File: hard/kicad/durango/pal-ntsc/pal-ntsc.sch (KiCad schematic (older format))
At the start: 34 parts, among them J101 SCART, J103 ~CSYNC, J4 S-Video, J5 COMPOSITE, Q1 BC548, Q2 BC548, Q3 BC548, U1 AD724, Y1 3.58 MHz (PAL=4.43)

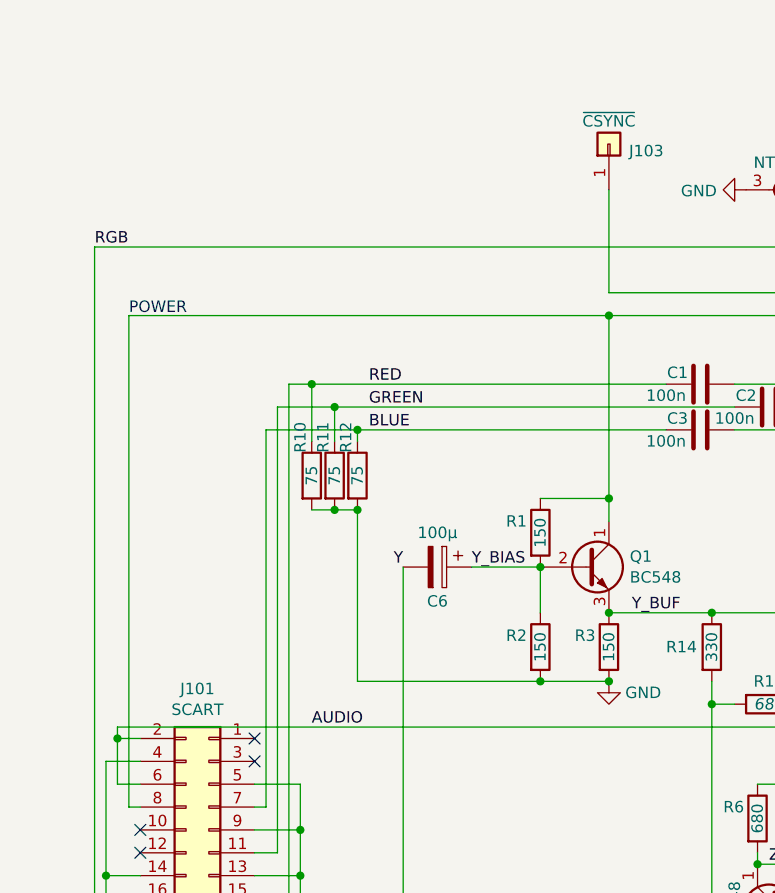
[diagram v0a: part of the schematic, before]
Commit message: preliminary PAL/NTSC encoder layout
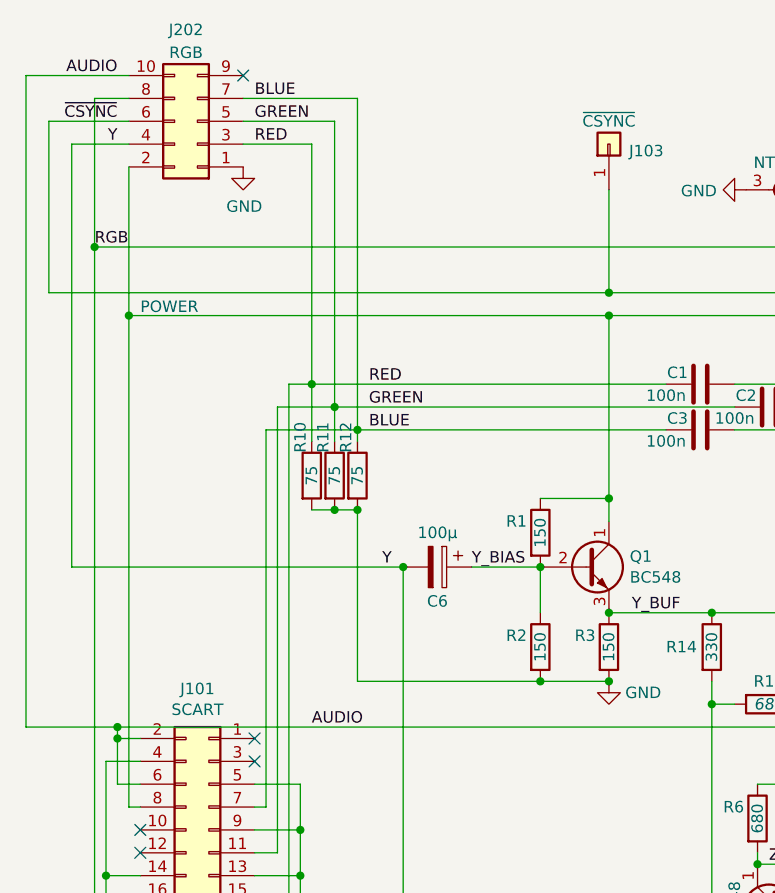
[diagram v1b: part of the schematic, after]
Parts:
- added J202: RGB, Connector_PinHeader_2.54mm:PinHeader_2x05_P2.54mm_Horizontal, symbol Connector_Generic:Conn_02x05_Odd_Even
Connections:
- net +5V: now also J202.2 (Pin_2)
- net AUDIO: now also J202.10 (Pin_10)
- net BLUE: now also J202.7 (Pin_7)
- net GND: now also J202.1 (Pin_1)
- net GREEN: now also J202.5 (Pin_5)
- net RED: now also J202.3 (Pin_3)
- net RGB: now also J202.8 (Pin_8)
- net Y: now also J202.4 (Pin_4)
- net ~CSYNC: now reaches J103.1 (Pin_1), U1.16 (HSYNC)
- net ~CSYNC: now also J202.6 (Pin_6)
- no-connect marks 7 -> 8
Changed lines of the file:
@@
 Wire Wire Line
 	3750 3700 4050 3700
-Text Label 3450 3700 2    50   ~ 0
+Text Label 3400 3700 2    50   ~ 0
 Y
 Text Label 4450 3900 0    50   ~ 0
@@
 Text Label 2100 2300 0    50   ~ 0
 RGB
-Text Notes 2250 2600 0    50   ~ 0
+Text Notes 2300 2600 0    50   ~ 0
 POWER
+$Comp
+L Connector_Generic:Conn_02x05_Odd_Even J202
+U 1 1 66483205
+P 2550 1750
+F 0 "J202" H 2600 1350 50  0000 C CNN
+F 1 "RGB" H 2600 1450 50  0000 C CNN
+F 2 "Connector_PinHeader_2.54mm:PinHeader_2x05_P2.54mm_Horizontal" H 2550 1750 50  0001 C CNN
+F 3 "~" H 2550 1750 50  0001 C CNN
+	1    2550 1750
+	-1   0    0    1
+$EndComp
+$Comp
+L power:GND #PWR?
+U 1 1 664B4163
+P 2750 1950
+F 0 "#PWR?" H 2750 1700 50  0001 C CNN
+F 1 "GND" H 2755 1777 50  0000 C CNN
+F 2 "" H 2750 1950 50  0001 C CNN
+F 3 "" H 2750 1950 50  0001 C CNN
+	1    2750 1950
+	1    0    0    -1
+$EndComp
+Wire Wire Line
+	3050 2900 3050 1850
+Wire Wire Line
+	3050 1850 2750 1850
+Wire Wire Line
+	2750 1750 3150 1750
+Wire Wire Line
+	3150 1750 3150 3000
+Wire Wire Line
+	3250 3100 3250 1650
+Wire Wire Line
+	3250 1650 2750 1650
+NoConn ~ 2750 1550
+Wire Wire Line
+	2250 1850 2000 1850
+Wire Wire Line
+	2000 1850 2000 3700
+Wire Wire Line
+	2000 3700 3450 3700
+Connection ~ 3450 3700
+Text Label 2200 1850 2    50   ~ 0
+Y
+Text Label 2800 1850 0    50   ~ 0
+RED
+Text Label 2800 1750 0    50   ~ 0
+GREEN
+Text Label 2800 1650 0    50   ~ 0
+BLUE
+Wire Wire Line
+	2250 1750 1900 1750
+Wire Wire Line
+	1900 1750 1900 2500
+Wire Wire Line
+	1900 2500 4350 2500
+Connection ~ 4350 2500
+Text Label 2200 1750 2    50   ~ 0
+~CSYNC
+Wire Wire Line
+	2250 1950 2250 2600
+Connection ~ 2250 2600
+Wire Wire Line
+	2100 2300 2100 1650
+Wire Wire Line
+	2100 1650 2250 1650
+Connection ~ 2100 2300
+Text Label 2200 1550 2    50   ~ 0
+AUDIO
+Wire Wire Line
+	2200 4400 1800 4400
+Wire Wire Line
+	1800 4400 1800 1550
+Wire Wire Line
+	1800 1550 2250 1550
+Connection ~ 2200 4400
 $EndSCHEMATC
